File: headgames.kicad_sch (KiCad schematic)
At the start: 39 parts, among them J1 ELECTRODES, U1 LM324N, U2 LM386

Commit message: Stabilize LM386 output with series Zobel network
Add C16 at 50 nF and R20 at 10 ohms as a series branch from LM386 pin 5 to ground, matching the output stabilization network in the manufacturer's gain-20 application. Branch before the speaker coupling capacitor so the network damps high-frequency load reactance without placing DC across the speaker or turning C16 into a direct capacitive output load.

Extend manage.py verification to require C16 on the amplifier output net, the isolated C16/R20 midpoint, R20's ground return, and the authoritative 50 nF and 10 ohm values. This prevents topology regressions such as a parallel RC branch or a capacitor connected directly from output to ground.

Verified with the root manage.py test using the project-local uv cache, KiCad 9 netlist export and ERC, rendered schematic inspection, and git diff checking. ERC remains limited to the two pre-existing undriven VCC/GND power-net errors.
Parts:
- added C16: 50n ZOBEL, symbol Device:C
- added R20: 10 ZOBEL, symbol Device:R
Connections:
- net GND: now also R20.2
- net at C15.1, U2.5: now also C16.1
- new net: C16.2, R20.1
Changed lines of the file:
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@@
 	(wire
 		(pts
-			(xy 248.92 78.74) (xy 257.81 78.74)
+			(xy 248.92 78.74) (xy 254 78.74)
+		)
+		(stroke
+			(width 0)
+			(type default)
+		)
+	)
+	(wire
+		(pts
+			(xy 254 78.74) (xy 257.81 78.74)
 		)
 		(stroke
@@
 	(wire
 		(pts
-			(xy 274.32 107.95) (xy 238.76 107.95)
+			(xy 274.32 107.95) (xy 254 107.95)
+		)
+		(stroke
+			(width 0)
+			(type default)
+		)
+	)
+	(wire
+		(pts
+			(xy 254 107.95) (xy 238.76 107.95)
 		)
 		(stroke
@@
 		(pts
 			(xy 76.2 86.36) (xy 101.6 86.36)
+		)
+		(stroke
+			(width 0)
+			(type default)
+		)
+	)
+	(wire
+		(pts
+			(xy 254 78.74) (xy 254 87.63)
+		)
+		(stroke
+			(width 0)
+			(type default)
+		)
+	)
+	(wire
+		(pts
+			(xy 254 95.25) (xy 254 99.06)
+		)
+		(stroke
+			(width 0)
+			(type default)
+		)
+	)
+	(wire
+		(pts
+			(xy 254 106.68) (xy 254 107.95)
 		)
 		(stroke
@@
 					(unit 1)
 				)
+			)
+		)
+	)
+	(symbol
+		(lib_id "Device:C")
+		(at 254 91.44 0)
+		(unit 1)
+		(exclude_from_sim no)
+		(in_bom yes)
+		(on_board yes)
+		(dnp no)
+		(property "Reference" "C16"
+			(at 256.921 90.2716 0)
+			(effects
+				(font
+					(size 1.27 1.27)
+				)
+				(justify left)
+			)
+		)
+		(property "Value" "50n ZOBEL"
+			(at 256.921 92.583 0)
+			(effects
+				(font
+					(size 1.27 1.27)
+				)
+				(justify left)
+			)
+		)
+		(property "Footprint" ""
+			(at 254 91.44 0)
+			(effects
+				(font
+					(size 1.27 1.27)
+				)
+			)
+		)
+		(property "Datasheet" ""
+			(at 254 91.44 0)
+			(effects
+				(font
+					(size 1.27 1.27)
+				)
+			)
+		)
+		(property "Description" ""
+			(at 254 91.44 0)
+			(effects
+				(font
+					(size 1.27 1.27)
+				)
+			)
+		)
+		(pin "1"
+		)
+		(pin "2"
+		)
+		(instances
+			(project "headgames"
+				(path "/16bca6b0-2f64-4676-a185-d512cb0de7e5"
+					(reference "C16")
+					(unit 1)
+				)
+			)
+		)
+	)
+	(symbol
+		(lib_id "Device:R")
+		(at 254 102.87 0)
+		(unit 1)
+		(exclude_from_sim no)
+		(in_bom yes)
+		(on_board yes)
+		(dnp no)
+		(property "Reference" "R20"
+			(at 256.921 101.7016 0)
+			(effects
+				(font
+					(size 1.27 1.27)
+				)
+				(justify left)
+			)
+		)
+		(property "Value" "10 ZOBEL"
+			(at 256.921 104.013 0)
+			(effects
+				(font
+					(size 1.27 1.27)
+				)
+				(justify left)
+			)
+		)
+		(property "Footprint" ""
+			(at 254 102.87 0)
+			(effects
+				(font
+					(size 1.27 1.27)
+				)
+			)
+		)
+		(property "Datasheet" ""
+			(at 254 102.87 0)
+			(effects
+				(font
+					(size 1.27 1.27)
+				)
+			)
+		)
+		(property "Description" ""
+			(at 254 102.87 0)
+			(effects
+				(font
+					(size 1.27 1.27)
+				)
+			)
+		)
+		(pin "1"
+		)
+		(pin "2"
+		)
+		(instances
+			(project "headgames"
+				(path "/16bca6b0-2f64-4676-a185-d512cb0de7e5"
+					(reference "R20")
+					(unit 1)
+				)

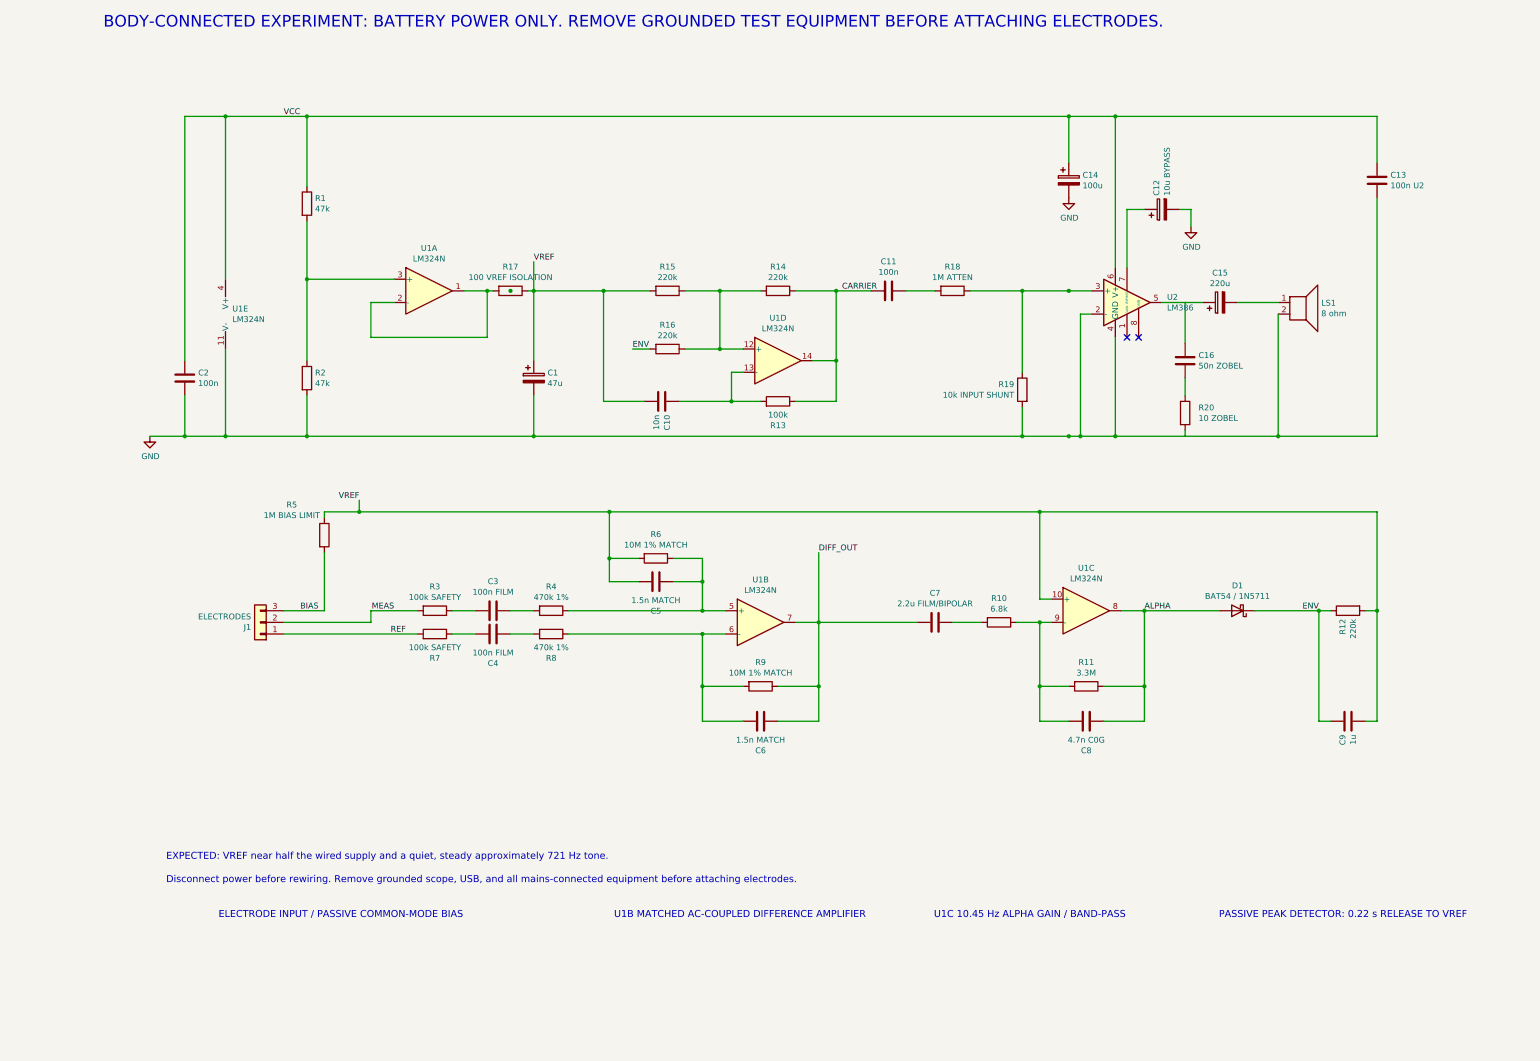
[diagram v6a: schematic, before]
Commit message: Define the isolated 9 V battery power contract
Replace the schematic's ambiguous loose VCC and ground stubs with a keyed three-position J2 battery interface. Pin 1 is the positive 9 V feed, pin 3 is battery return, and pin 2 is deliberately unused as a polarization key. Add source flags at the connector-fed rails so KiCad ERC can distinguish an intentional external source from an accidentally undriven power network.

Make the operating voltage and isolation requirement explicit in both the connector metadata and the on-sheet safety notes. This removes guesswork around LM324 headroom, LM386 supply range, capacitor polarity, and electrode bias-current bounds while retaining the project's battery-only body-connection invariant.

Extend the root manage.py verification entrypoint to prove the J2 pin assignment, nominal isolated-battery value, unused key pin, and a clean full KiCad ERC result. The native schematic now exports successfully, all project engineering checks pass, and KiCad reports zero ERC violations.
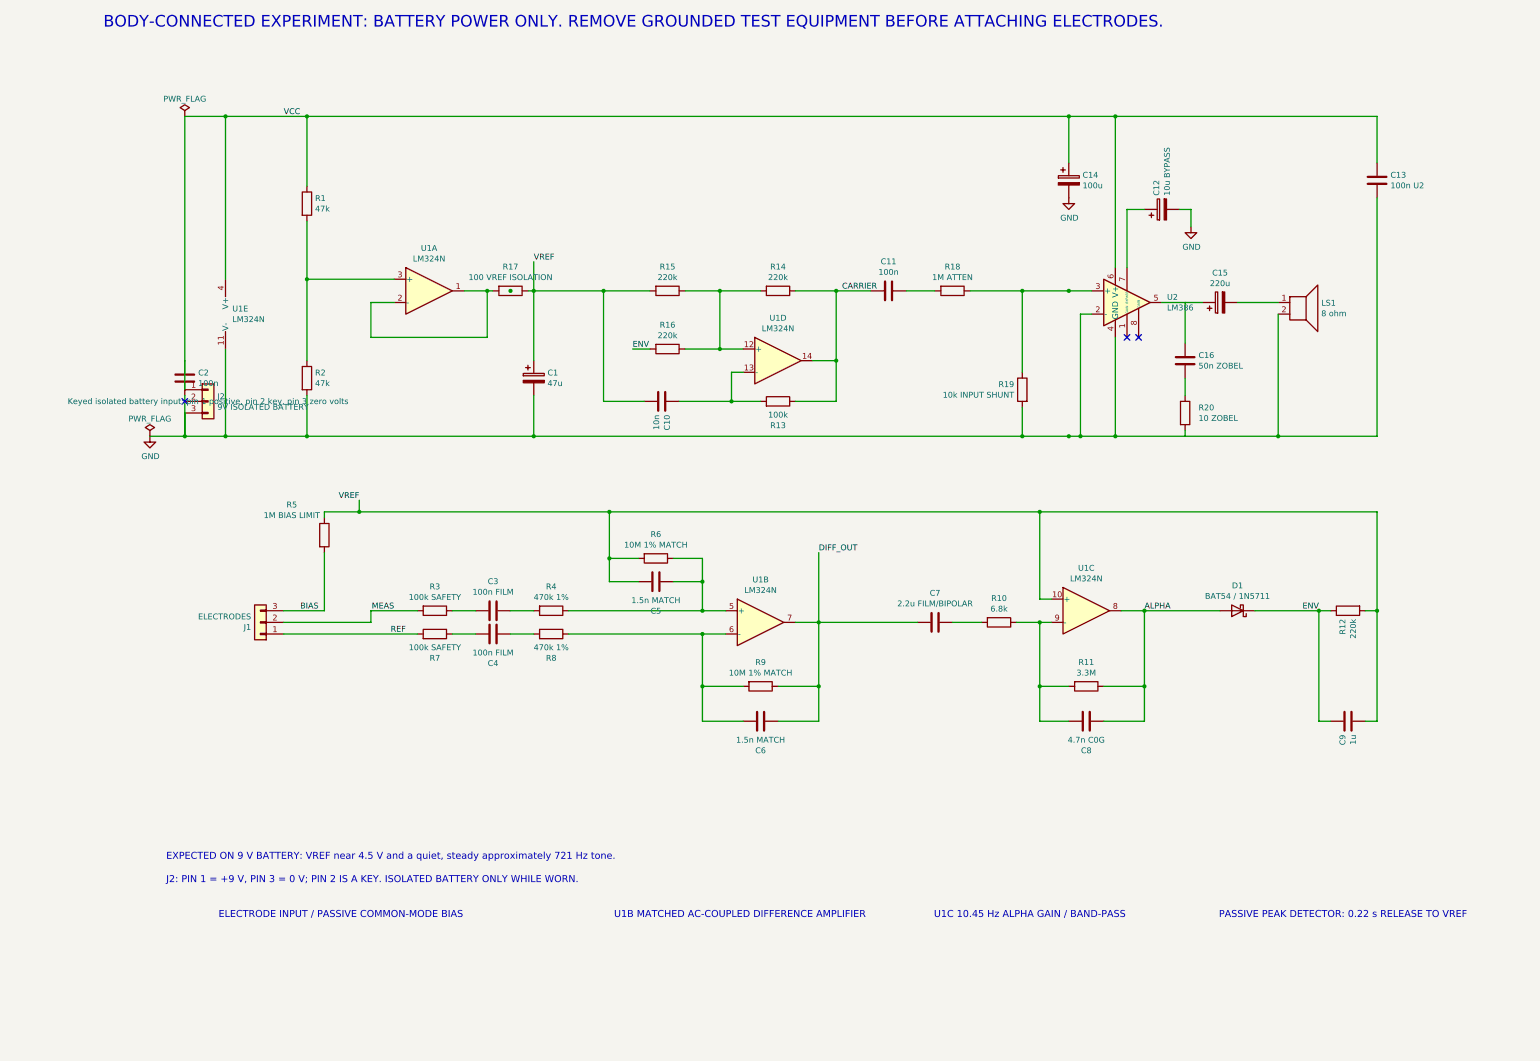
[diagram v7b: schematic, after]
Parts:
- added J2: 9V ISOLATED BATTERY, symbol Connector_Generic:Conn_01x03
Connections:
- net GND: now also J2.3 (Pin_3)
- net VCC: now also J2.1 (Pin_1)
- no-connect marks 2 -> 3
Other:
- note added: "EXPECTED ON 9 V BATTERY: VREF near 4.5 V and a quiet, steady approximately 721 Hz tone."
- note added: "J2: PIN 1 = +9 V, PIN 3 = 0 V; PIN 2 IS A KEY. ISOLATED BATTERY ONLY WHILE WORN."
- note removed: "Disconnect power before rewiring. Remove grounded scope, USB, and all mains-connected equipment before attaching electrodes."
- note removed: "EXPECTED: VREF near half the wired supply and a quiet, steady approximately 721 Hz tone."
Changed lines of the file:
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@@
 		)
 	)
-	(text "EXPECTED: VREF near half the wired supply and a quiet, steady approximately 721 Hz tone."
+	(text "EXPECTED ON 9 V BATTERY: VREF near 4.5 V and a quiet, steady approximately 721 Hz tone."
 		(exclude_from_sim no)
 		(at 31.496 200.66 0)
@@
 		)
 	)
-	(text "Disconnect power before rewiring. Remove grounded scope, USB, and all mains-connected equipment before attaching electrodes."
+	(text "J2: PIN 1 = +9 V, PIN 3 = 0 V; PIN 2 IS A KEY. ISOLATED BATTERY ONLY WHILE WORN."
 		(exclude_from_sim no)
 		(at 31.496 205.74 0)
@@
 		(at 243.84 86.36)
 	)
+	(no_connect
+		(at 35.56 100.33)
+	)
+	(wire
+		(pts
+			(xy 35.56 91.44) (xy 35.56 97.79)
+		)
+		(stroke (width 0) (type default))
+	)
+	(wire
+		(pts
+			(xy 35.56 102.87) (xy 35.56 107.95)
+		)
+		(stroke (width 0) (type default))
+	)
 	(wire
 		(pts
@@
 					(unit 1)
 				)
+			)
+		)
+	)
+	(symbol
+		(lib_id "Connector_Generic:Conn_01x03")
+		(at 40.64 100.33 0)
+		(unit 1)
+		(exclude_from_sim no)
+		(in_bom yes)
+		(on_board yes)
+		(dnp no)
+		(property "Reference" "J2"
+			(at 42.672 99.2632 0)
+			(effects (font (size 1.27 1.27)) (justify left))
+		)
+		(property "Value" "9V ISOLATED BATTERY"
+			(at 42.672 101.5746 0)
+			(effects (font (size 1.27 1.27)) (justify left))
+		)
+		(property "Footprint" ""
+			(at 40.64 100.33 0)
+			(effects (font (size 1.27 1.27)))
+		)
+		(property "Datasheet" ""
+			(at 40.64 100.33 0)
+			(effects (font (size 1.27 1.27)))
+		)
+		(property "Description" "Keyed isolated battery input: pin 1 positive, pin 2 key, pin 3 zero volts"
+			(at 40.64 100.33 0)
+			(effects (font (size 1.27 1.27)))
+		)
+		(pin "1")
+		(pin "2")
+		(pin "3")
+		(instances
+			(project "headgames"
+				(path "/16bca6b0-2f64-4676-a185-d512cb0de7e5"
+					(reference "J2")
+					(unit 1)
+				)
+			)
+		)
+	)
+	(symbol
+		(lib_id "power:PWR_FLAG")
+		(at 35.56 38.1 0)
+		(unit 1)
+		(exclude_from_sim no)
+		(in_bom yes)
+		(on_board yes)
+		(dnp no)
+		(property "Reference" "#FLG0101"
+			(at 35.56 36.195 0)
+			(effects (font (size 1.27 1.27)) (hide yes))
+		)
+		(property "Value" "PWR_FLAG"
+			(at 35.56 34.29 0)
+			(effects (font (size 1.27 1.27)))
+		)
+		(property "Footprint" ""
+			(at 35.56 38.1 0)
+			(effects (font (size 1.27 1.27)) (hide yes))
+		)
+		(property "Datasheet" "~"
+			(at 35.56 38.1 0)
+			(effects (font (size 1.27 1.27)) (hide yes))
+		)
+		(property "Description" ""
+			(at 35.56 38.1 0)
+			(effects (font (size 1.27 1.27)) (hide yes))
+		)
+		(pin "1")
+		(instances
+			(project "headgames"
+				(path "/16bca6b0-2f64-4676-a185-d512cb0de7e5"
+					(reference "#FLG0101")
+					(unit 1)
+				)
+			)
+		)
+	)
+	(symbol
+		(lib_id "power:PWR_FLAG")
+		(at 27.94 107.95 0)
+		(unit 1)
+		(exclude_from_sim no)
+		(in_bom yes)
+		(on_board yes)
+		(dnp no)
+		(property "Reference" "#FLG0102"
+			(at 27.94 106.045 0)
+			(effects (font (size 1.27 1.27)) (hide yes))
+		)
+		(property "Value" "PWR_FLAG"
+			(at 27.94 104.14 0)
+			(effects (font (size 1.27 1.27)))
+		)
+		(property "Footprint" ""
+			(at 27.94 107.95 0)
+			(effects (font (size 1.27 1.27)) (hide yes))
+		)
+		(property "Datasheet" "~"
+			(at 27.94 107.95 0)
+			(effects (font (size 1.27 1.27)) (hide yes))
+		)
+		(property "Description" ""
+			(at 27.94 107.95 0)
+			(effects (font (size 1.27 1.27)) (hide yes))
+		)
+		(pin "1")
+		(instances
+			(project "headgames"
+				(path "/16bca6b0-2f64-4676-a185-d512cb0de7e5"
+					(reference "#FLG0102")
+					(unit 1)
+				)

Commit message: Harden the physiological pickup and alpha detector path
Replace the authoritative LM324N population with the pin-compatible TLC274CN low-bias CMOS quad amplifier. The 9 V single-supply topology and existing package boundary remain intact, while picoamp-scale input bias avoids the large 10 MΩ acquisition-network error inherent to the bipolar LM324. Retain LM324 only as an explicitly documented artifact-test fallback rather than the physiological pickup configuration.

Separate the U1C alpha-band corners by changing C7 to 2.7 uF and C8 to 3.9 nF. With the existing 6.8 kΩ input and 3.3 MΩ feedback resistors, the calculated high-pass and low-pass corners are 8.67 Hz and 12.36 Hz instead of two interacting poles near 10.5 Hz. This gives the analog path a real, auditable alpha passband.

Resolve the detector's ambiguous BAT54-or-1N5711 callout in favor of the 1N5711 zero-bias detector specified for low-level RF-style detection. Preserve the deliberate 220 ms R12/C9 release to VREF.

Expand manage.py to parse capacitances, enforce all paired difference-amplifier R/C matches, require the low-bias quad and selected detector, calculate and bound both alpha corners, and verify the envelope release constant. Update the project architecture and README so these decisions remain authoritative after context clearing.

Verification: python3 manage.py test passes; kicad-cli ERC reports zero violations; native netlist and PDF exports succeed; git diff --check passes.
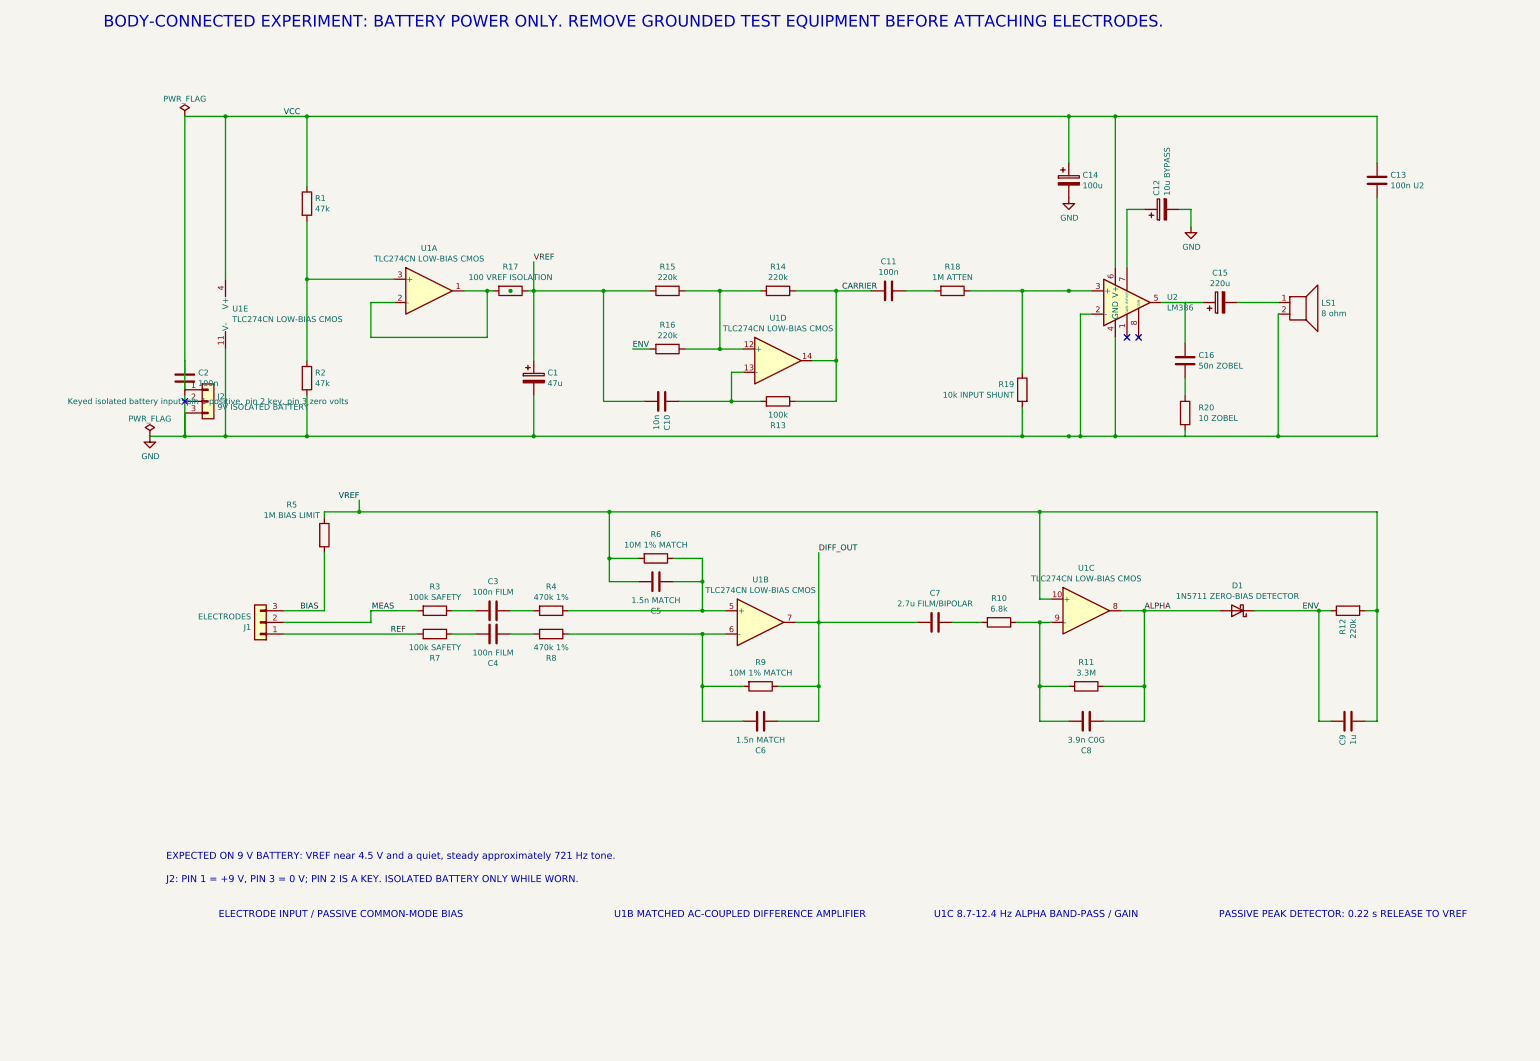
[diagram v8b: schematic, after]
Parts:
- C7: value 2.2u FILM/BIPOLAR -> 2.7u FILM/BIPOLAR
- C8: value 4.7n C0G -> 3.9n C0G
- D1: value BAT54 / 1N5711 -> 1N5711 ZERO-BIAS DETECTOR
- U1: value LM324N -> TLC274CN LOW-BIAS CMOS
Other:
- note added: "U1C 8.7-12.4 Hz ALPHA BAND-PASS / GAIN"
- note removed: "U1C 10.45 Hz ALPHA GAIN / BAND-PASS"
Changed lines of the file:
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@@
 		(company "Headgames")
 		(comment 1 "BATTERY ONLY WHILE ELECTRODES ARE CONNECTED")
-		(comment 2 "LM324 reference and carrier into LM386 speaker amplifier")
+		(comment 2 "TLC274CN reference, acquisition, alpha gain, and carrier")
 		(comment 3 "Pins 1 and 8 of LM386 intentionally open for gain 20")
 		(comment 4 "Experimental prototype - not a medical device")
@@
 		)
 	)
-	(text "U1C 10.45 Hz ALPHA GAIN / BAND-PASS"
+	(text "U1C 8.7-12.4 Hz ALPHA BAND-PASS / GAIN"
 		(exclude_from_sim no)
 		(at 199.136 213.36 0)
@@
 			)
 		)
-		(property "Value" "LM324N"
+		(property "Value" "TLC274CN LOW-BIAS CMOS"
 			(at 88.9 69.1896 0)
 			(effects
@@
 			)
 		)
-		(property "Value" "LM324N"
+		(property "Value" "TLC274CN LOW-BIAS CMOS"
 			(at 165.1 84.4296 0)
 			(effects
@@
 			)
 		)
-		(property "Value" "LM324N"
+		(property "Value" "TLC274CN LOW-BIAS CMOS"
 			(at 45.9232 82.423 0)
 			(effects
@@
 			)
 		)
-		(property "Value" "LM324N"
+		(property "Value" "TLC274CN LOW-BIAS CMOS"
 			(at 161.29 141.5796 0)
 			(effects
@@
 			)
 		)
-		(property "Value" "2.2u FILM/BIPOLAR"
+		(property "Value" "2.7u FILM/BIPOLAR"
 			(at 199.39 144.5006 90)
 			(effects
@@
 			)
 		)
-		(property "Value" "LM324N"
+		(property "Value" "TLC274CN LOW-BIAS CMOS"
 			(at 232.41 139.0396 0)
 			(effects
@@
 			)
 		)
-		(property "Value" "4.7n C0G"
+		(property "Value" "3.9n C0G"
 			(at 232.41 174.2694 90)
 			(effects
@@
 			)
 		)
-		(property "Value" "BAT54 / 1N5711"
+		(property "Value" "1N5711 ZERO-BIAS DETECTOR"
 			(at 265.43 142.875 0)
 			(effects
